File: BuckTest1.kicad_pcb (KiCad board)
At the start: 2 copper layers, 50.8 x 25.4 mm, 23 parts, among them J1 POWERCONN, J2 POWERCONN, U1 LM3102

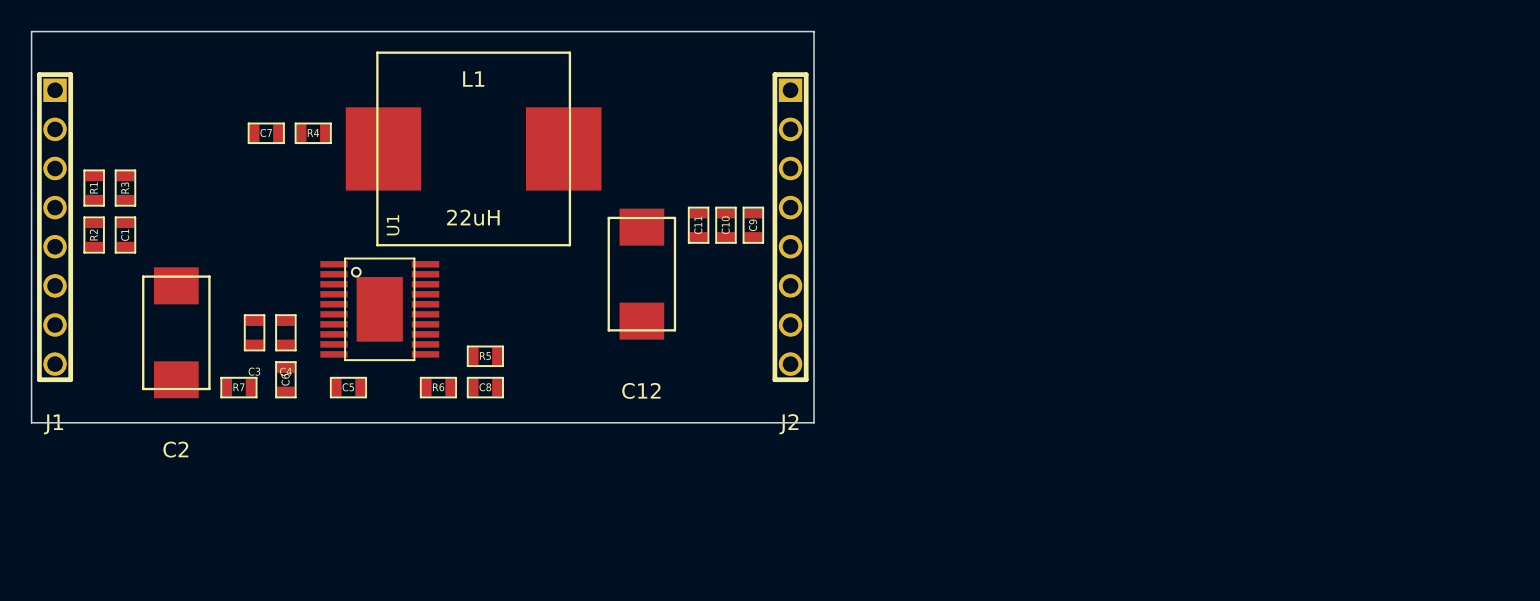
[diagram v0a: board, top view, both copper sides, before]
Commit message: Copper layout complete
Hand routed first board to test KiCad layout features. .dsn an .ses are
autoroute files. Initial copper layout complete, could use improvements
but will function.
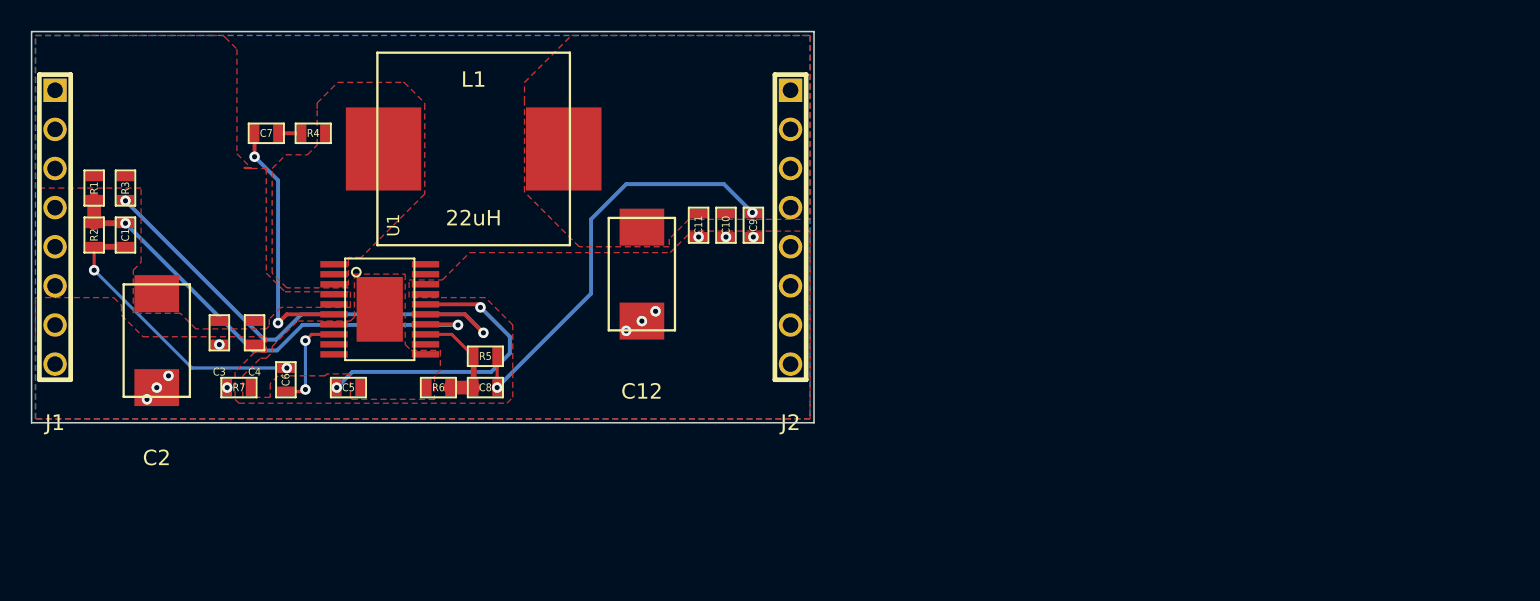
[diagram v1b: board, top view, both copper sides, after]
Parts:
- moved C3 2.29 mm to (89.2, 103.6)
- moved C4 2.03 mm to (91.4, 103.6)
- moved C2 1.37 mm to (85.1, 104.1)
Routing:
- net N-000007: track 0.00 -> 32.5 mm, vias 0 -> 2
- net /Buck_EN: track 0.00 -> 31.4 mm, vias 0 -> 2
- net /PP3V3OUT: track 0.00 -> 27.8 mm, vias 0 -> 2
- net N-000003: track 0.00 -> 19.6 mm, vias 0 -> 2
- net AGND: track 0.00 -> 18.8 mm, vias 0 -> 2
- net N-000005: track 0.00 -> 16.8 mm, vias 0 -> 2
- net GND: track 0.00 -> 13.1 mm, vias 0 -> 11
- net /Buck_FB: track 0.00 -> 7.27 mm
- net N-000004: track 0.00 -> 6.52 mm, vias 0 -> 2
- net N-000001: track 0.00 -> 1.52 mm
- added copper zone on F.Cu, net /Buck_SW
- added copper zone on F.Cu, net /PP12VIN
- added copper zone on F.Cu, net /PP3V3OUT
- added copper zone on F.Cu, net AGND
- added copper zone on B.Cu, net GND
- added copper zone on F.Cu, net GND
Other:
- net class Default: via_dia 0.635 -> 0.6858; via_drill 0.508 -> 0.3302
- rule via_min_size: 0.3302 -> 0.6858

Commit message: BuckConverterTest V0
Silkscreen complete
Sent for fab to OSH Park
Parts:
- moved C10 46.1 mm to (167.1, 106.2)
- moved C11 46.1 mm to (165.4, 106.2)
- moved C2 46.1 mm to (130.2, 113.7)
- moved C3 46.1 mm to (134.2, 113.2)
- moved C4 46.1 mm to (136.5, 113.2)
- moved C5 46.1 mm to (142.6, 116.7)
- moved C7 46.1 mm to (137.3, 100.2)
- moved J2 46.1 mm to (171.3, 106.3)
- moved R1 46.1 mm to (126.1, 103.8)
- moved R2 46.1 mm to (126.1, 106.8)
- moved R4 46.1 mm to (140.3, 100.2)
- moved C1 46.1 mm to (128.1, 106.8)
- moved C12 46.1 mm to (161.7, 109.3)
- moved C6 46.1 mm to (138.6, 116.2)
- moved C8 46.1 mm to (151.5, 116.7)
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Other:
- board text added: "GND"
- board text added: "Vin"
- board text added: "Vout"
